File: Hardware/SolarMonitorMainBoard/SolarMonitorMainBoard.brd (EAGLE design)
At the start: 100 x 78.7 mm, 50 parts, among them K1 RT314F12, K2 RT314F12, K3 RT314F12, U1 INA219AIDR, U10 TSR_1-2450, U2 INA219AIDR, U3 INA219AIDR, U4 INA219AIDR, U5 INA219AIDR, U6 INA219AIDR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

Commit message: Some Routing
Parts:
- removed R14, R8: (no value), SparkFun-Resistors:0805
- added R13, R42: (no value), SparkFun-Resistors:0805
- moved R11 68.6 mm to (71.6, 27.9)
- moved D1 19.3 mm to (32.0, 50.0)
- moved R23 10.4 mm to (74.7, 19.1), turned to 90 degrees
- moved D23 9.89 mm to (77.2, 18.8), turned to 270 degrees
- moved R12 9.67 mm to (71.6, 23.5), turned to 180 degrees
- moved J3 8.52 mm to (80.9, 8.76), turned to 270 degrees
- moved D21 6.23 mm to (77.1, 26.8), turned to 270 degrees
- moved R6 5.97 mm to (97.4, 19.1)
- moved D22 4.85 mm to (77.2, 22.4), turned to 270 degrees
- moved R21 3.14 mm to (74.8, 27.1), turned to 90 degrees
- moved R22 2.81 mm to (74.7, 22.6), turned to 90 degrees
- renumbered R10 to R41
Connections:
- net FONA_RX: now also J2.13; no longer J2.15
- net FONA_TX: now also J2.15; no longer J2.13
- net GND: now also R21.1, R22.1, R23.1; no longer R12.1, R14.1, R8.1
- net LIN1SENSE: now also R12.2; no longer R22.2
- net LIN2SENSE: now also R13.2; no longer R23.2
- net LOUT+: now also R11.2; no longer R21.2
- net N$2: now also R11.1, R21.2; no longer R21.1, R8.2
- net N$38: now also R12.1, R22.2; no longer R12.2, R22.1
- net N$40: now also R13.1, R23.2; no longer R14.2, R23.1
- net SDA: now also R42.2; no longer R11.2
- net VCC: now also R42.1; no longer R11.1
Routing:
- net SDA: track 4.84 -> 62.5 mm, vias 0 -> 2
- net 5V: track 0.00 -> 25.8 mm
- net FONA_RX: track 0.00 -> 17.6 mm
- net FONA_TX: track 0.00 -> 10.7 mm
- net VCC: track 134.5 -> 129.3 mm

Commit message: Fix  checks
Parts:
- moved U$1 0.18 mm to (85.1, 16.9)
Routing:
- net LOUT-: track 15.2 -> 59.6 mm
- net VI: track 67.2 -> 62.4 mm
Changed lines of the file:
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@@
 <param name="RoutingGrid" value="50mil"/>
 <param name="AutoGrid" value="1"/>
-<param name="Efforts" value="1"/>
+<param name="Efforts" value="2"/>
 <param name="TopRouterVariant" value="1"/>
 <param name="tpViaShape" value="round"/>
@@
 </element>
 <element name="U10" library="_traco_tsr-1" package="TSR-1" value="TSR_1-2450" x="6.858" y="63.373"/>
-<element name="U$1" library="adafruit" package="MICROSD" value="MICROSD" x="85.217" y="16.764"/>
+<element name="U$1" library="adafruit" package="MICROSD" value="MICROSD" x="85.09" y="16.891"/>
 <element name="D1" library="SparkFun-DiscreteSemi" package="SOD-523" value="RB751" x="32.004" y="50.038" rot="R270">
 <attribute name="PROD_ID" value="DIO-11018" x="32.004" y="50.038" size="1.778" layer="27" rot="R270" display="off"/>
@@
 <vertex x="-1.27" y="-2.54"/>
 </polygon>
-<via x="18.415" y="31.623" extent="1-16" drill="0.6"/>
-<via x="23.495" y="31.623" extent="1-16" drill="0.6"/>
-<via x="41.275" y="31.623" extent="1-16" drill="0.6"/>
-<via x="33.655" y="31.623" extent="1-16" drill="0.6"/>
-<via x="30.226" y="30.48" extent="1-16" drill="0.6"/>
+<via x="18.415" y="31.623" extent="1-16" drill="0.6" shape="octagon"/>
+<via x="23.495" y="31.623" extent="1-16" drill="0.6" shape="octagon"/>
+<via x="41.275" y="31.623" extent="1-16" drill="0.6" shape="octagon"/>
+<via x="33.655" y="31.623" extent="1-16" drill="0.6" shape="octagon"/>
+<via x="29.083" y="29.845" extent="1-16" drill="0.6" shape="octagon"/>
 <contactref element="U7" pad="5"/>
 <contactref element="U7" pad="3"/>
-<via x="53.467" y="31.242" extent="1-16" drill="0.6"/>
+<via x="53.467" y="31.242" extent="1-16" drill="0.6" shape="octagon"/>
 <contactref element="C7" pad="1"/>
 <contactref element="X6" pad="1"/>
-<via x="8.509" y="27.051" extent="1-16" drill="0.6"/>
+<via x="8.509" y="27.051" extent="1-16" drill="0.6" shape="octagon"/>
 <wire x1="39.889" y1="44.069" x2="40.005" y2="46.4312" width="0.254" layer="1"/>
 <contactref element="X3" pad="3"/>
@@
 <wire x1="30.48" y1="64.516" x2="43.18" y2="55.88" width="0" layer="19" extent="1-1"/>
 <wire x1="84.72" y1="27.559" x2="70.993" y2="34.798" width="0" layer="19" extent="1-1"/>
-<wire x1="98.309" y1="19.05" x2="95.9866" y2="25.127" width="0" layer="19" extent="1-1"/>
-<wire x1="90.917" y1="5.724" x2="98.309" y2="19.05" width="0" layer="19" extent="1-1"/>
+<wire x1="98.309" y1="19.05" x2="98.298" y2="25.157" width="0" layer="19" extent="1-1"/>
+<wire x1="90.79" y1="5.851" x2="98.309" y2="19.05" width="0" layer="19" extent="1-1"/>
 </signal>
 <signal name="SCL">
@@
 <wire x1="43.053" y1="30.226" x2="42.037" y2="30.226" width="0.254" layer="1"/>
 <via x="42.037" y="30.226" extent="1-16" drill="0.6" shape="octagon"/>
-<wire x1="42.037" y1="30.226" x2="26.543" y2="30.226" width="0.254" layer="16"/>
+<wire x1="42.037" y1="30.226" x2="28.829" y2="30.988" width="0.254" layer="16"/>
+<wire x1="28.829" y1="30.988" x2="26.543" y2="30.226" width="0.254" layer="16"/>
 <via x="26.543" y="30.226" extent="1-16" drill="0.6" shape="octagon"/>
 <wire x1="58.547" y1="32.0548" x2="58.547" y2="30.734" width="0.254" layer="1"/>
@@
 <wire x1="40.386" y1="40.64" x2="41.275" y2="41.402" width="0.254" layer="1"/>
 <wire x1="41.275" y1="41.402" x2="41.275" y2="46.4312" width="0.254" layer="1"/>
-<wire x1="97.79" y1="44.0436" x2="96.52" y2="39.37" width="0.8128" layer="1"/>
 <wire x1="4.318" y1="63.373" x2="4.318" y2="44.704" width="0.8128" layer="1"/>
 <wire x1="4.318" y1="44.704" x2="9.271" y2="40.64" width="0.8128" layer="1"/>
 <wire x1="9.271" y1="40.64" x2="39.11" y2="40.64" width="0.8128" layer="1"/>
-<wire x1="41.275" y1="41.402" x2="96.52" y2="39.37" width="0" layer="19" extent="1-1"/>
+<wire x1="41.275" y1="46.4312" x2="97.79" y2="44.0436" width="0" layer="19" extent="1-1"/>
 </signal>
 <signal name="5V">
@@
 <contactref element="U$1" pad="2"/>
 <contactref element="MS1" pad="22"/>
-<wire x1="20.32" y1="35.56" x2="93.117" y2="6.524" width="0" layer="19" extent="1-1"/>
+<wire x1="20.32" y1="35.56" x2="92.99" y2="6.651" width="0" layer="19" extent="1-1"/>
 </signal>
 <signal name="SCK">
@@
 <contactref element="J2" pad="12"/>
 <wire x1="20.32" y1="61.976" x2="20.32" y2="55.88" width="0.254" layer="16"/>
-<wire x1="20.32" y1="55.88" x2="89.817" y2="6.124" width="0" layer="19" extent="1-1"/>
+<wire x1="20.32" y1="55.88" x2="89.69" y2="6.251" width="0" layer="19" extent="1-1"/>
 </signal>
 <signal name="MOSI">
@@
 <contactref element="J2" pad="14"/>
 <wire x1="17.78" y1="61.976" x2="17.78" y2="55.88" width="0.254" layer="16"/>
-<wire x1="17.78" y1="55.88" x2="92.017" y2="6.124" width="0" layer="19" extent="1-1"/>
+<wire x1="17.78" y1="55.88" x2="91.89" y2="6.251" width="0" layer="19" extent="1-1"/>
 </signal>
 <signal name="MISO">
@@
 <contactref element="J2" pad="16"/>
 <wire x1="15.24" y1="61.976" x2="15.24" y2="55.88" width="0.254" layer="16"/>
-<wire x1="15.24" y1="55.88" x2="87.617" y2="6.124" width="0" layer="19" extent="1-1"/>
+<wire x1="15.24" y1="55.88" x2="87.49" y2="6.251" width="0" layer="19" extent="1-1"/>
 </signal>
 <signal name="SD_CARD_DETECT">
 <contactref element="MS1" pad="20"/>
 <contactref element="U$1" pad="CD1"/>
-<wire x1="15.24" y1="35.56" x2="87.217" y2="16.324" width="0" layer="19" extent="1-1"/>
+<wire x1="15.24" y1="35.56" x2="87.09" y2="16.451" width="0" layer="19" extent="1-1"/>
 </signal>
 <signal name="FONA_RX">
@@
 <wire x1="66.802" y1="70.739" x2="63.119" y2="75.438" width="3.81" layer="1"/>
 <wire x1="63.119" y1="75.438" x2="54.737" y2="75.438" width="3.81" layer="1"/>
-<wire x1="54.737" y1="75.438" x2="54.737" y2="74.5998" width="3.81" layer="1"/>
+<wire x1="54.737" y1="75.438" x2="54.737" y2="75.184" width="3.81" layer="1"/>
 <contactref element="X6" pad="6"/>
-<wire x1="12.8481" y1="74.524" x2="54.737" y2="75.438" width="0" layer="19" extent="1-1"/>
+<wire x1="54.737" y1="75.184" x2="54.737" y2="74.5998" width="3.81" layer="1"/>
+<wire x1="12.8481" y1="74.524" x2="14.478" y2="77.343" width="0.8128" layer="1"/>
+<wire x1="14.478" y1="77.343" x2="52.451" y2="77.343" width="0.8128" layer="1"/>
+<wire x1="52.451" y1="77.343" x2="54.737" y2="75.184" width="0.8128" layer="1"/>
 </signal>
 <signal name="LIN1" class="1">
@@
 <wire x1="74.549" y1="64.262" x2="74.422" y2="70.739" width="3.81" layer="16"/>
 <wire x1="82.139" y1="53.28" x2="74.579" y2="53.28" width="3.81" layer="16"/>
-<wire x1="74.579" y1="53.28" x2="69.85" y2="48.26" width="0.8128" layer="1"/>
-<wire x1="69.85" y1="48.26" x2="58.42" y2="39.37" width="0.8128" layer="1"/>
+<wire x1="74.579" y1="53.28" x2="69.596" y2="48.641" width="0.8128" layer="1"/>
+<wire x1="69.596" y1="48.641" x2="58.42" y2="39.37" width="0.8128" layer="1"/>
 <wire x1="58.42" y1="39.37" x2="55.88" y2="39.37" width="0.8128" layer="1"/>
 <wire x1="55.88" y1="39.37" x2="54.61" y2="40.64" width="0.8128" layer="1"/>
@@
 <contactref element="R6" pad="1"/>
 <wire x1="96.509" y1="19.05" x2="92.094" y2="21.2344" width="0" layer="19" extent="1-1"/>
-<wire x1="79.629" y1="7.493" x2="96.509" y2="19.05" width="0" layer="19" extent="1-1"/>
+<wire x1="79.629" y1="7.493" x2="92.094" y2="21.2344" width="0" layer="19" extent="1-1"/>
 <wire x1="22.86" y1="35.56" x2="79.629" y2="7.493" width="0" layer="19" extent="1-1"/>
 </signal>

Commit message: More routing
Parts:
- turned R11 to 180 degrees
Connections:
- removed net SLAVE_GND: J3.6
- removed net SLAVE_VCC: J3.2
- net GND: now also J3.6
- net N$30: now also U7.22; no longer U7.19
- net N$31: now also U7.19; no longer U7.22
- net VCC: now also J3.2
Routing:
- net VCC: track 129.3 -> 184.4 mm, vias 0 -> 2
- net LOUT+: track 14.7 -> 56.8 mm, vias 0 -> 1
- net SLAVE_RX: track 0.00 -> 40.4 mm, vias 0 -> 1
- net SLAVE_TX: track 0.00 -> 39.7 mm
- net SLAVE_MOSI: track 0.00 -> 24.5 mm, vias 0 -> 1
- net SLAVE_MISO: track 0.00 -> 22.6 mm, vias 0 -> 1
- net N$30: track 0.00 -> 22.5 mm
- net N$31: track 0.00 -> 22.1 mm
- net N$2: track 0.00 -> 18.1 mm
- net N$40: track 0.00 -> 17.4 mm
- net LIN1SENSE: track 0.00 -> 16.4 mm
- net N$38: track 0.00 -> 15.2 mm
- net N$3: track 0.00 -> 5.72 mm
- net N$10: track 0.00 -> 5.47 mm
- net N$21: track 0.00 -> 5.21 mm
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
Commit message: All routed. Let's check.
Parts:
- moved R6 22.7 mm to (77.3, 8.51), turned to 90 degrees
- moved D1 18.9 mm to (27.4, 68.3), turned to 0 degrees
- moved C8 3.05 mm to (98.4, 27.3), turned to 270 degrees
- moved R21 1.33 mm to (74.4, 28.3)
- moved D21 1.33 mm to (76.7, 28.1)
- moved D22 1.33 mm to (76.8, 23.6)
- moved D23 1.33 mm to (76.8, 20.1)
- moved R11 1.33 mm to (71.2, 29.2)
- moved R12 1.33 mm to (71.2, 24.8)
- moved R13 1.33 mm to (71.2, 21.2)
- moved R22 1.33 mm to (74.3, 23.9)
- moved R23 1.33 mm to (74.3, 20.3)
- moved U$1 0.51 mm to (85.1, 17.4)
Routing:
- net T_A_B: track 0.00 -> 214.0 mm, vias 0 -> 1
- net T_ON_OFF: track 0.00 -> 212.4 mm, vias 0 -> 1
- net SLAVE_NOTIFY: track 0.00 -> 167.1 mm, vias 0 -> 2
- net SD_CS: track 0.00 -> 160.0 mm, vias 0 -> 2
- net MOSI: track 6.10 -> 165.7 mm
- net SCK: track 6.10 -> 163.2 mm
- net MISO: track 6.10 -> 157.7 mm, vias 0 -> 2
- net SLAVE_EXT_IO: track 0.00 -> 129.4 mm, vias 0 -> 2
- net VCC: track 184.4 -> 299.9 mm, vias 2 -> 5
- net SCL: track 66.4 -> 176.0 mm, vias 3 -> 5
- net OUT_12V_2: track 0.00 -> 107.3 mm, vias 0 -> 2
- net SLAVE_RESET: track 0.00 -> 104.1 mm, vias 0 -> 1
- net OUT_12V_1: track 0.00 -> 100.4 mm, vias 0 -> 2
- net SDA: track 62.5 -> 162.1 mm, vias 2 -> 6
- net SD_CARD_DETECT: track 0.00 -> 90.2 mm, vias 0 -> 1
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
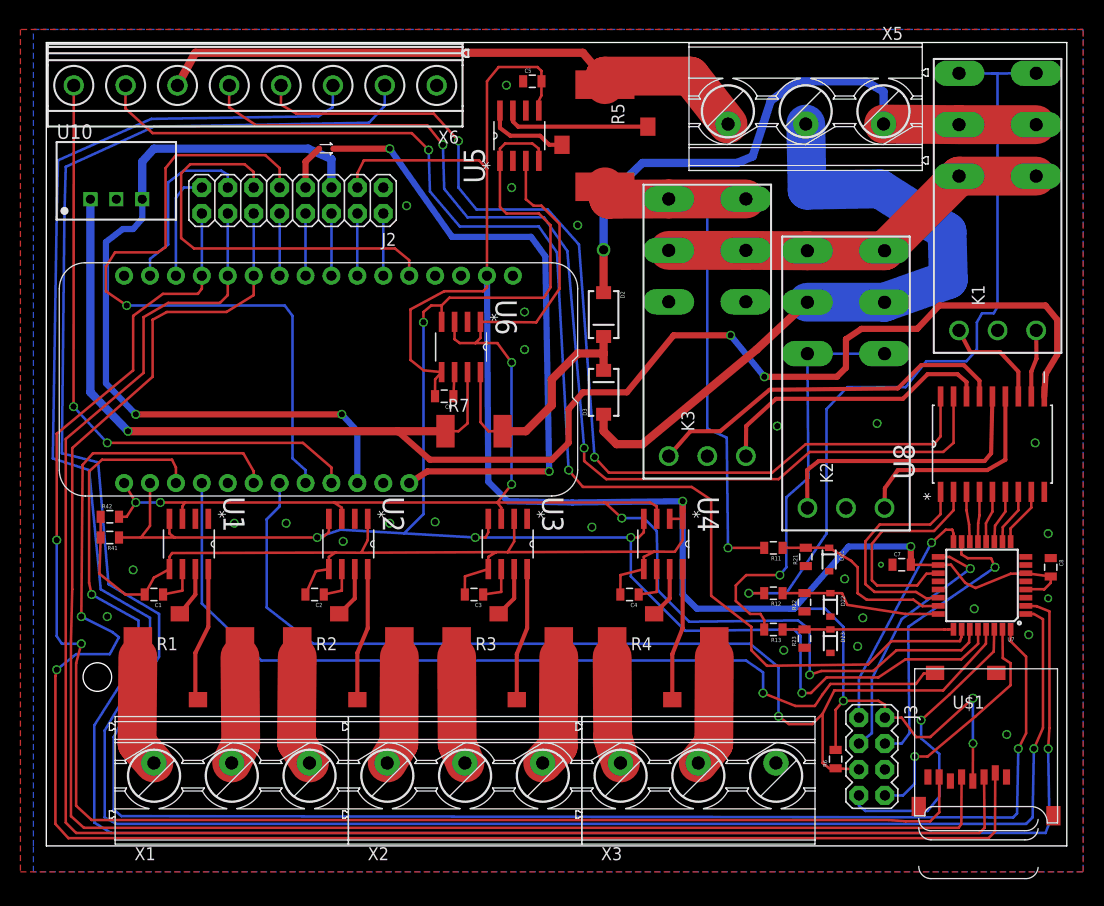
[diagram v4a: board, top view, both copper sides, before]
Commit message: Fix Warnings ADD I2C to header
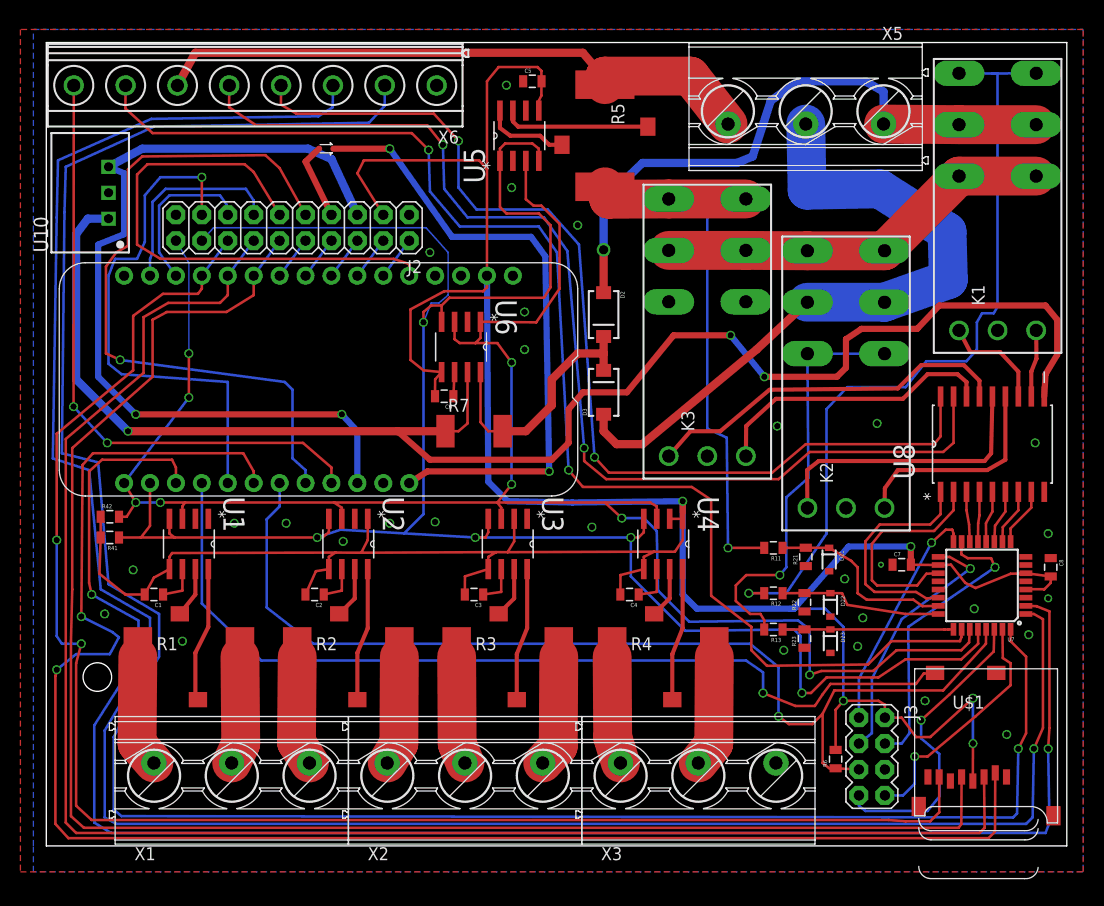
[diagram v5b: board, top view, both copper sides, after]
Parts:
- J2: device SparkFun-Connectors:2X8 -> SparkFun-Connectors:2X10
- moved J2 9.72 mm to (24.1, 60.6)
- moved U10 0.99 mm to (6.10, 64.0), turned to 90 degrees
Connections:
- net FONA_RST: now also J2.17
- net SCL: now also J2.18
- net SDA: now also J2.20
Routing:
- net FONA_RST: track 0.00 -> 51.0 mm, vias 0 -> 1
- net SCL: track 176.0 -> 209.9 mm
- net SDA: track 162.1 -> 188.4 mm, vias 6 -> 8
- net FONA_PS: track 40.3 -> 52.2 mm
- net 5V: track 77.7 -> 84.6 mm
- net FONA_TX: track 10.7 -> 15.9 mm
- net VCC: track 299.9 -> 303.3 mm
- net FONA_BAT: track 4.38 -> 7.63 mm
- net FONA_RX: track 17.6 -> 19.7 mm
- net SCK: track 163.2 -> 161.4 mm
- net MOSI: track 165.7 -> 163.8 mm
- net MISO: track 157.7 -> 155.8 mm
- net DISP_DC: track 6.10 -> 4.27 mm
- net DISP2_RST: track 6.10 -> 4.27 mm
- net DISP1_RST: track 6.10 -> 4.27 mm
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
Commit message: Cleanup
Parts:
- C1, C2, C3, C4, C5, C6: value (none) -> 0.1uF
- J2: value (none) -> ToTopPrint
- J3: value (none) -> ISP
- R41, R42: value (none) -> 10k
- R7: value (none) -> 100m
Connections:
- net VCC renamed 3V
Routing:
- net FONA_KEY: track 68.7 -> 70.8 mm
- net GND: vias 29 -> 30
